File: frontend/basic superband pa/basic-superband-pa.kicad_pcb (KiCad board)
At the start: 2 copper layers, 64.4 x 78.6 mm, 69 parts, among them CN1 EDGE, CN2 BREAKOUT, K1 D3002, K2 D3002, P1 BNC, P2 CONN_02X01, P3 CONN_01X02, Q1 NPN, Q2 PNP, Q3 RD16HHF1, Q4 NPN, T1 TRANSFO, T2 8:1, T3 4:1, T4 OUT_TRANSF, U1 LP2951-50D

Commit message: Upload latest pcb changes
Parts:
- removed CN2: BREAKOUT, Pin_Headers:Pin_Header_Straight_1x12
- removed MH (x4): VAL**, HERMESLITE:MH
- removed MountingHole_2-7mm: VAL**, Mounting_Holes:MountingHole_2-7mm
- removed P3: CONN_01X02, Pin_Headers:Pin_Header_Straight_1x02
- removed Q4: NPN, Transistors_SMD:sot23
- removed R9: 4.99k, HERMESLITE:R_0805
- added C25: 0.01uF, HERMESLITE:C_0805, B.Cu at (151.2, 73.2)
- added C26: 0.01uF, HERMESLITE:C_0805, B.Cu at (158.2, 84.4)
- added C27: 0.01uF, HERMESLITE:C_0805, B.Cu at (154.4, 72.2)
- added C28: 0.01uF, HERMESLITE:C_0805, F.Cu at (183.2, 54.8)
- added C29: 0.1uF, HERMESLITE:C_0805, B.Cu at (174.6, 68.3)
- added MountingHole_3-5mm: VAL**, Mounting_Holes:MountingHole_3-5mm, F.Cu at (189.8, 90.6)
- added MountingHole_3-5mm: VAL**, Mounting_Holes:MountingHole_3-5mm, F.Cu at (139.0, 90.6)
- added MountingHole_3-5mm: VAL**, Mounting_Holes:MountingHole_3-5mm, F.Cu at (189.6, 39.6)
- added MountingHole_3-5mm: VAL**, Mounting_Holes:MountingHole_3-5mm, F.Cu at (139.0, 39.4)
- added MountingHole_6mm: VAL**, Mounting_Holes:MountingHole_6mm, F.Cu at (154.4, 50.4)
- C1, C15, C16, C2, Q1, R1, R2, R5, R7: moved to B.Cu
- C12: moved to F.Cu
- L10: footprint Choke_Axial_ThroughHole:Choke_Horizontal_RM10mm -> Choke_Toroid_ThroughHole:Choke_Toroid_horizontal_Diameter3-5mm_Amidon-T12
- moved L5 38.7 mm to (184.0, 87.0), turned to 180 degrees
- moved L2 38.2 mm to (143.6, 73.4), turned to 270 degrees
- moved L10 34.5 mm to (186.6, 44.8)
- moved L3 32.1 mm to (142.2, 86.6)
- moved C7 31.9 mm to (146.6, 91.0)
- moved C6 31.5 mm to (142.8, 85.8)
- moved L6 30.6 mm to (190.4, 85.2), turned to 90 degrees
- moved L4 29.2 mm to (156.2, 87.0), turned to 180 degrees
- moved C8 28.7 mm to (182.2, 74.6)
- moved L7 27.4 mm to (170.0, 87.0), turned to 180 degrees
- moved C13 24.3 mm to (140.0, 61.8), turned to 90 degrees
- moved C5 24.2 mm to (146.8, 84.6)
- moved C4 23.8 mm to (151.4, 83.6), turned to 180 degrees
- moved C2 17.8 mm to (136.8, 73.6), turned to 270 degrees
- moved L1 17.5 mm to (158.6, 86.6), turned to 90 degrees
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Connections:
- CN1 pad A16: Net-(CN1-PadA15) -> Net-(CN1-PadA16)
- CN1 pad A18: Net-(CN1-PadA17) -> Net-(CN1-PadA18)
- K2 pad 7: Net-(C24-Pad2) -> Net-(C29-Pad1)
- R8 pad 2: Net-(Q4-Pad3) -> PTT#
- U1 pad 3: Net-(Q4-Pad3) -> PTT#
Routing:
- net PTT#: track 36.9 -> 88.3 mm, vias 1 -> 7
- net Net-(K1-Pad7): track 46.6 -> 14.6 mm, vias 1 -> 0
- net Net-(CN1-PadA17): track 30.6 -> 0.00 mm
- net Net-(CN1-PadA15): track 30.4 -> 0.00 mm
- net Net-(CN1-PadB14): track 23.9 -> 0.00 mm, vias 1 -> 0
- net Net-(CN1-PadB18): track 21.2 -> 0.00 mm
- net Net-(CN1-PadB13): track 20.8 -> 0.00 mm, vias 1 -> 0
- net Net-(CN1-PadB17): track 20.7 -> 0.00 mm
- net Net-(CN1-PadB16): track 19.9 -> 0.00 mm
- net Net-(CN1-PadB15): track 19.3 -> 0.00 mm
- net Net-(C19-Pad2): track 41.4 -> 23.1 mm
- net GPIO0: track 44.1 -> 26.0 mm, vias 2 -> 0
- net Net-(Q4-Pad3): track 17.5 -> 0.00 mm
- net Net-(CN1-PadB3): track 12.4 -> 29.4 mm
- net Net-(K1-Pad8): track 31.9 -> 15.9 mm
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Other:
- board size 64.4 x 78.6 mm -> 64.5 x 60 mm

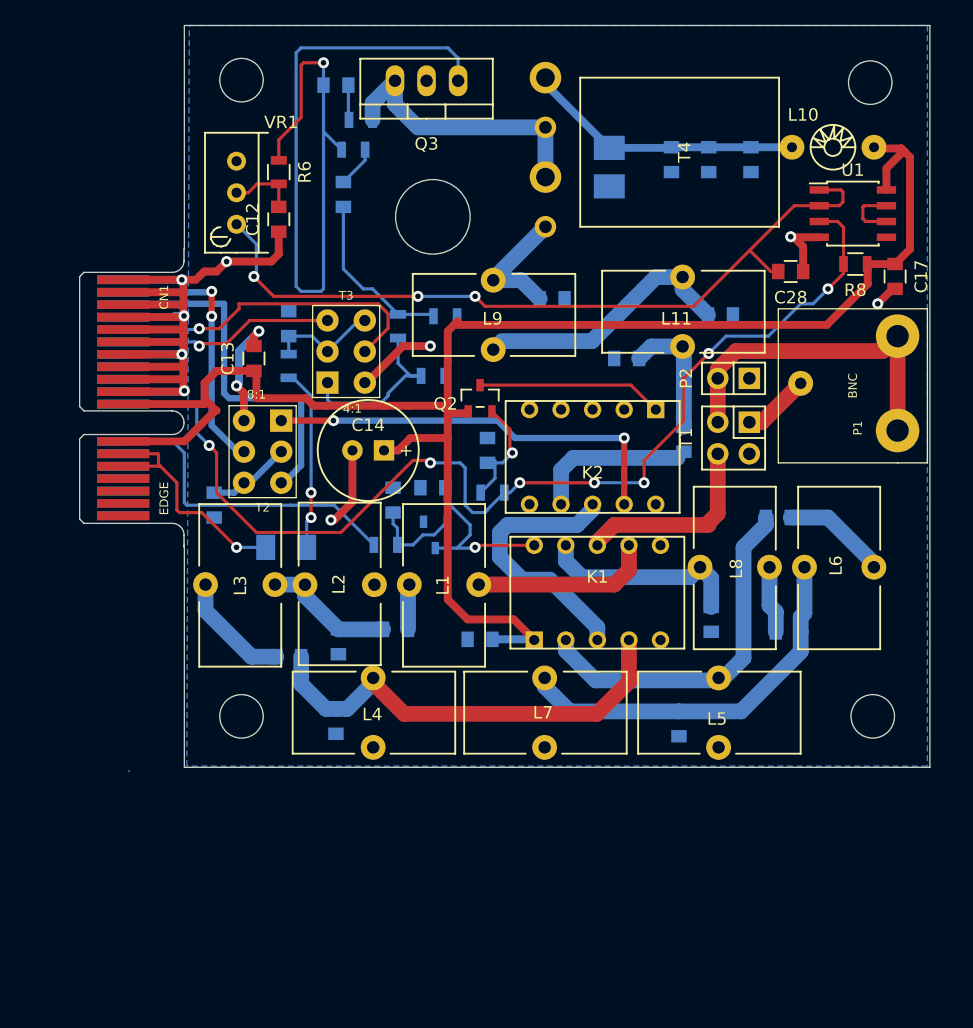
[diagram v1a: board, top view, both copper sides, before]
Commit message: Correct compnent naming and fix relay error
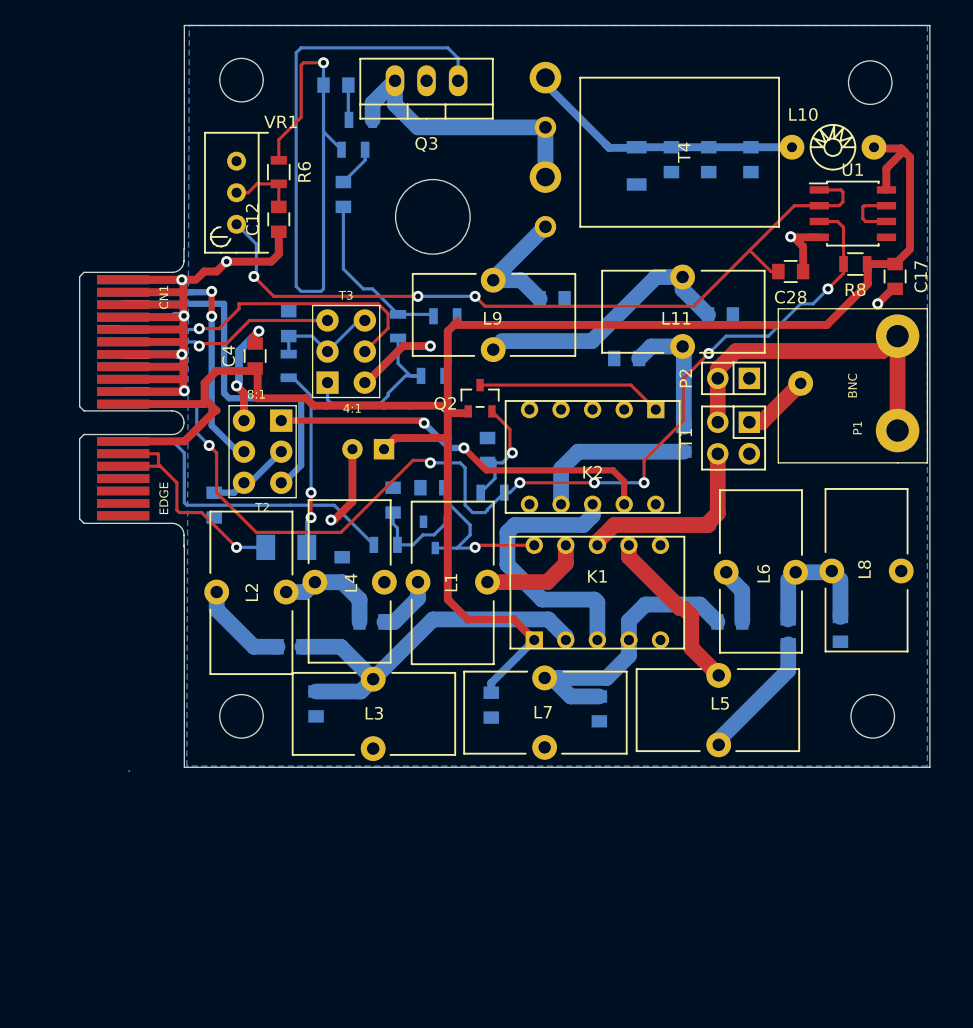
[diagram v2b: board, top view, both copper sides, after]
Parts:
- C13: value 0.1uF -> C; moved to B.Cu
- C14: value 47uF 16V -> C; footprint Discret:C1V8 -> HERMESLITE:C_0805; moved to B.Cu
- C22: footprint Capacitors_Tantalum_SMD:TantalC_SizeB_EIA-3528_Reflow -> Capacitors_SMD:C_1206
- C4: value C -> 0.1uF; moved to F.Cu
- C7: value C -> 47uF 16V; footprint HERMESLITE:C_0805 -> Discret:C1V8
- moved C13 52.0 mm to (187.2, 83.6), turned to 270 degrees
- moved C8 35.4 mm to (147.1, 78.8), turned to 90 degrees
- moved C9 29.2 mm to (145.0, 89.6)
- moved C14 27.9 mm to (167.8, 90.0), turned to 270 degrees
- moved C4 24.7 mm to (140.1, 61.6), turned to 90 degrees
- moved C7 22.1 mm to (149.2, 69.1), turned to 180 degrees
- moved L6 18.2 mm to (177.5, 72.4), turned to 270 degrees
- moved L4 18.2 mm to (144.4, 73.2), turned to 270 degrees
- moved L5 14.7 mm to (170.8, 93.4), turned to 0 degrees
- moved L3 14.0 mm to (156.2, 87.1), turned to 180 degrees
- moved L2 13.8 mm to (143.1, 87.2), turned to 90 degrees
- moved L8 13.5 mm to (186.0, 72.3), turned to 270 degrees
- moved C26 5.38 mm to (159.1, 89.7), turned to 90 degrees
- moved C5 3.14 mm to (149.5, 83.0), turned to 180 degrees
- moved C22 2.20 mm to (170.8, 46.3)
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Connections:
- C11 pad 2: GND -> Net-(C11-Pad2)
- C13 pad 1: Net-(C13-Pad1) -> Net-(C10-Pad1)
- C14 pad 1: Net-(C13-Pad1) -> Net-(C11-Pad1)
- C17 pad 1: Net-(C13-Pad1) -> Net-(C17-Pad1)
- C26 pad 2: Net-(C13-Pad1) -> Net-(C17-Pad1)
- C4 pad 1: Net-(C4-Pad1) -> Net-(C17-Pad1)
- C4 pad 2: Net-(C4-Pad2) -> GND
- C5 pad 1: Net-(C4-Pad2) -> Net-(C5-Pad1)
- C5 pad 2: GND -> Net-(C5-Pad2)
- C7 pad 1: Net-(C6-Pad2) -> Net-(C17-Pad1)
- C8 pad 1: Net-(C8-Pad1) -> Net-(C5-Pad2)
- C8 pad 2: Net-(C8-Pad2) -> GND
- C9 pad 1: Net-(C10-Pad1) -> Net-(C6-Pad2)
- CN1 pad A11: Net-(C13-Pad1) -> Net-(C17-Pad1)
- CN1 pad A12: Net-(C13-Pad1) -> Net-(C17-Pad1)
- K1 pad 1: Net-(C13-Pad1) -> Net-(C17-Pad1)
- K1 pad 2: Net-(C8-Pad1) -> Net-(C6-Pad2)
- K1 pad 4: Net-(C6-Pad2) -> Net-(C11-Pad1)
- K1 pad 9: Net-(C11-Pad1) -> Net-(K1-Pad9)
- L1 pad 1: Net-(K1-Pad7) -> Net-(K1-Pad9)
- L1 pad 2: Net-(C4-Pad1) -> Net-(C5-Pad1)
- L10 pad 1: Net-(C13-Pad1) -> Net-(C17-Pad1)
- L2 pad 1: Net-(C4-Pad2) -> Net-(C5-Pad2)
- L2 pad 2: GND -> Net-(C6-Pad1)
- L3 pad 1: Net-(C4-Pad2) -> Net-(C6-Pad2)
- L3 pad 2: Net-(C6-Pad1) -> GND
- L4 pad 1: Net-(C6-Pad2) -> Net-(C5-Pad2)
- L5 pad 1: Net-(C8-Pad1) -> Net-(C10-Pad2)
- L5 pad 2: GND -> Net-(K1-Pad7)
- L6 pad 1: Net-(C8-Pad2) -> Net-(C11-Pad2)
- L7 pad 1: Net-(C10-Pad1) -> Net-(C11-Pad1)
- L8 pad 1: Net-(C10-Pad2) -> Net-(C10-Pad1)
- L8 pad 2: Net-(C11-Pad1) -> GND
- Q2 pad 1: Net-(C13-Pad1) -> Net-(C17-Pad1)
- R8 pad 1: Net-(C13-Pad1) -> Net-(C17-Pad1)
- U1 pad 8: Net-(C13-Pad1) -> Net-(C17-Pad1)
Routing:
- net Net-(C17-Pad1): track 0.00 -> 139.9 mm
- net Net-(C13-Pad1): track 137.1 -> 0.00 mm
- net Net-(C8-Pad1): track 28.9 -> 0.00 mm
- net Net-(C10-Pad1): track 31.0 -> 11.0 mm
- net Net-(C4-Pad2): track 10.7 -> 0.00 mm
- net Net-(C5-Pad2): track 0.00 -> 8.91 mm
- net Net-(K1-Pad9): track 0.00 -> 8.66 mm
- net Net-(C8-Pad2): track 8.53 -> 0.00 mm
- net Net-(C11-Pad1): track 16.5 -> 23.6 mm
- net Net-(C6-Pad2): track 35.7 -> 30.1 mm
- net Net-(C10-Pad2): track 5.41 -> 10.4 mm
- net Net-(C5-Pad1): track 0.00 -> 4.79 mm
- net Net-(C11-Pad2): track 0.00 -> 4.53 mm
- net Net-(C4-Pad1): track 3.65 -> 0.00 mm
- net Net-(K2-Pad9): track 33.5 -> 31.5 mm
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
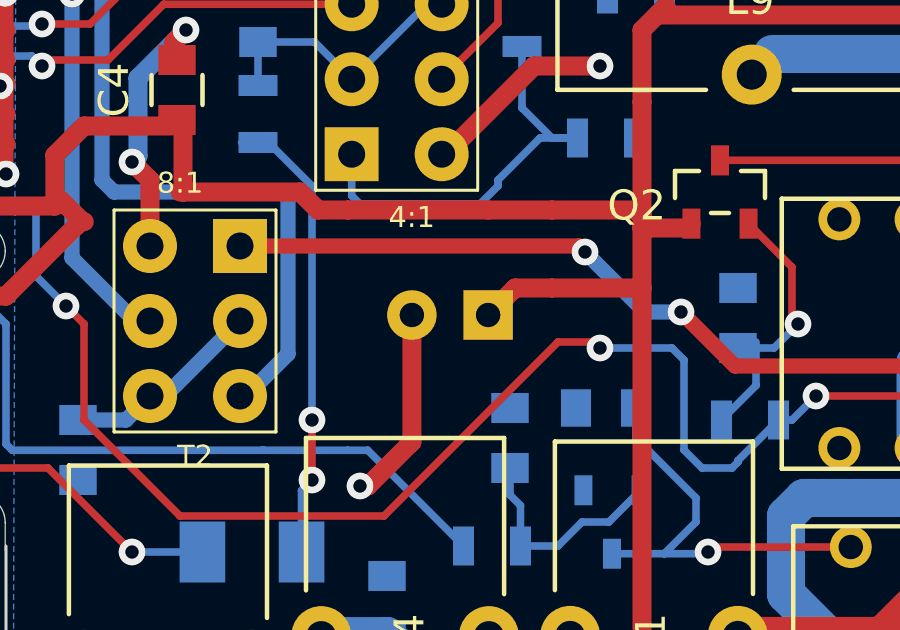
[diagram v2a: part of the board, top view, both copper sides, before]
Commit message: Minor silkscreen bug
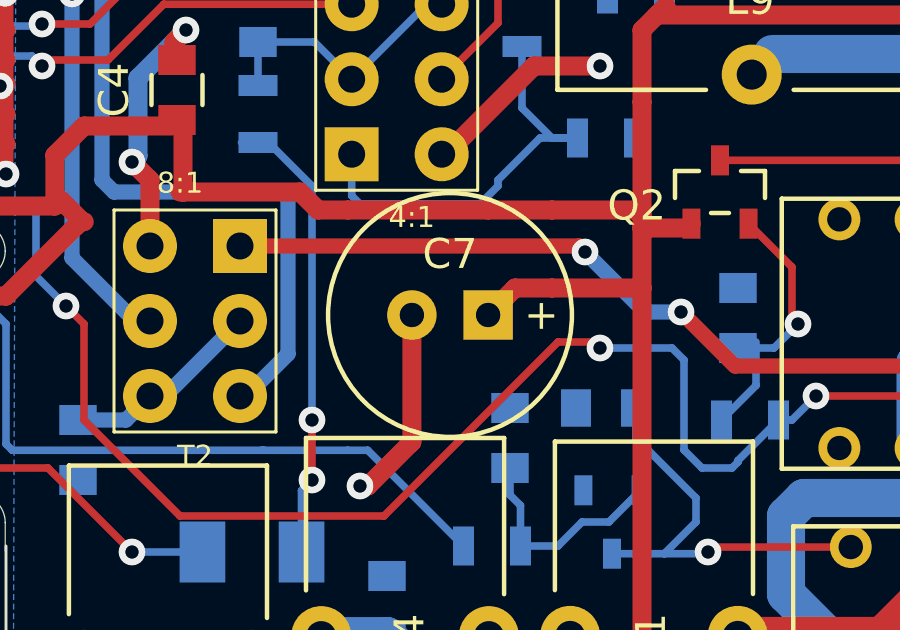
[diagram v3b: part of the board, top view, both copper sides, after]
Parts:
- C7: moved to F.Cu
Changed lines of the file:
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@@
     (links 138)
     (no_connects 0)
-    (area 129.98958 34.949999 194.450001 95.056161)
+    (area 125.47056 33.72012 198.438524 96.969)
     (thickness 1.6)
     (drawings 6)
@@
     )
   )
-  (module Discret:C1V8 (layer B.Cu)
+  (module Discret:C1V8 (layer F.Cu)
     (at 149.2 69.1 180)
-    (fp_text reference C7 (at 0 -2.032 180) (layer B.SilkS)
-      (effects (font (size 1 1) (thickness 0.15)) (justify mirror))
-    )
-    (fp_text value "47uF 16V" (at 0 1.77546 270) (layer B.SilkS)
-      (effects (font (size 1 1) (thickness 0.15)) (justify mirror))
-    )
-    (fp_text user + (at -3.04546 0 180) (layer B.SilkS)
-      (effects (font (size 1 1) (thickness 0.15)) (justify mirror))
-    )
-    (fp_circle (center 0 0) (end 4.064 0) (layer B.SilkS) (width 0.15))
-    (pad 1 thru_hole rect (at -1.27 0 180) (size 1.651 1.651) (drill 0.8128) (layers *.Cu *.Mask B.SilkS)
+    (fp_text reference C7 (at 0 2.032 180) (layer F.SilkS)
+      (effects (font (size 1 1) (thickness 0.15)))
+    )
+    (fp_text value "47uF 16V" (at 0 -1.77546 450) (layer F.SilkS) hide
+      (effects (font (size 1 1) (thickness 0.15)))
+    )
+    (fp_text user + (at -3.04546 0 180) (layer F.SilkS)
+      (effects (font (size 1 1) (thickness 0.15)))
+    )
+    (fp_circle (center 0 0) (end 4.064 0) (layer F.SilkS) (width 0.15))
+    (pad 1 thru_hole rect (at -1.27 0 180) (size 1.651 1.651) (drill 0.8128) (layers *.Cu *.Mask F.SilkS)
       (net 57 "Net-(C17-Pad1)"))
-    (pad 2 thru_hole circle (at 1.27 0 180) (size 1.651 1.651) (drill 0.8128) (layers *.Cu *.Mask B.SilkS)
+    (pad 2 thru_hole circle (at 1.27 0 180) (size 1.651 1.651) (drill 0.8128) (layers *.Cu *.Mask F.SilkS)
       (net 2 GND))
     (model Discret/C1V8.wrl
@@
     (tags "capacitor 1206")
     (attr smd)
-    (fp_text reference C22 (at 0 2.3 270) (layer B.SilkS)
-      (effects (font (size 1 1) (thickness 0.15)) (justify mirror))
-    )
-    (fp_text value "10uF 16V" (at 0 -2.3 270) (layer B.SilkS)
-      (effects (font (size 1 1) (thickness 0.15)) (justify mirror))
-    )
+    (fp_text reference C22 (at 4 -0.1 270) (layer B.SilkS)
+      (effects (font (size 1 1) (thickness 0.15)) (justify mirror))
+    )
+    (fp_text value "10uF 16V" (at 0 -2.3 270) (layer B.SilkS) hide
+      (effects (font (size 1 1) (thickness 0.15)) (justify mirror))
+    )

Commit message: Final PCB, hopefully
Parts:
- added G***: OSHW-logo_copper-front_3mm, OSHW:OSHW-logo_copper-front_3mm, F.Cu at (184.1, 39.5)
- moved R12 7.56 mm to (158.5, 65.3)
- moved L9 6.21 mm to (160.6, 51.7), turned to 270 degrees
- moved R11 5.40 mm to (151.4, 64.6)
- moved C18 5.00 mm to (164.2, 62.0)
- moved MountingHole_6mm 4.41 mm to (154.7, 54.8)
- moved R10 2.01 mm to (154.2, 65.2)
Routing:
- net Net-(C15-Pad2): track 13.8 -> 24.3 mm
- net Net-(C23-Pad2): track 21.6 -> 13.0 mm
- net GND: track 119.9 -> 127.4 mm, vias 11 -> 12
- net Net-(R10-Pad2): track 14.7 -> 9.88 mm
- net Net-(C28-Pad2): track 62.6 -> 65.4 mm, vias 3 -> 1
- net Net-(C18-Pad2): track 10.4 -> 12.6 mm
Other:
- net class Microstrip: trace_width 3.81 -> 0.381
- board text added: "Hermes Lite Superband PA 1.0 © 2015 AC9HY"

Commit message: More pcb changes
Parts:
- C15, C16, R5, R7: moved to F.Cu
- moved R7 7.56 mm to (155.5, 45.7)
- moved C16 6.59 mm to (151.0, 44.7)
- moved C8 4.39 mm to (146.2, 83.1), turned to 270 degrees
- moved C6 2.69 mm to (141.0, 86.9)
- moved FB1 1.40 mm to (142.6, 75.6)
- moved C15 0.94 mm to (147.7, 49.4)
- moved MountingHole_6mm 0.81 mm to (153.9, 54.7)
- moved R5 0.76 mm to (147.7, 45.7), turned to 270 degrees
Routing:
- net GND: track 127.4 -> 107.7 mm, vias 12 -> 9
- net Net-(C15-Pad2): track 24.3 -> 35.5 mm, vias 0 -> 1
- net Net-(C28-Pad2): track 65.4 -> 61.0 mm
- net Net-(C17-Pad1): track 139.9 -> 136.7 mm
- net Net-(C5-Pad2): track 8.91 -> 11.7 mm
- net Net-(C16-Pad2): track 67.9 -> 70.2 mm, vias 1 -> 2
- net Net-(C15-Pad1): track 3.37 -> 1.75 mm
- net Net-(K1-Pad3): track 22.9 -> 21.3 mm
- net GPIO0: track 26.0 -> 24.7 mm, vias 0 -> 2
- net Net-(C6-Pad2): track 30.1 -> 31.3 mm
- net Net-(FB1-Pad2): track 15.3 -> 14.2 mm, vias 2 -> 0
- net Net-(Q3-Pad3): track 22.7 -> 21.7 mm
- net PTT#: track 88.3 -> 89.3 mm, vias 7 -> 8

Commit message: Few more pcb changes
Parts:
- added JP1: JUMPER4, HERMESLITE:JUMPER4, F.Cu at (156.2, 90.4)
- added R13: 4.99k, HERMESLITE:R_0805, B.Cu at (162.4, 89.0)
- moved C26 7.56 mm to (156.5, 82.6), turned to 0 degrees
- moved L7 4.01 mm to (174.0, 86.7)
- moved C14 3.91 mm to (171.7, 89.7)
- moved L5 3.20 mm to (174.0, 93.3)
- moved C6 2.81 mm to (140.8, 84.1)
- moved L3 1.58 mm to (154.7, 86.6)
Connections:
- R1 pad 2: GPIO0 -> Net-(JP1-Pad2)
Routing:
- net Net-(JP1-Pad2): track 0.00 -> 23.6 mm, vias 0 -> 1
- net GPIO0: track 24.7 -> 45.7 mm, vias 2 -> 3
- net Net-(C17-Pad1): track 136.7 -> 141.8 mm
- net Net-(C11-Pad1): track 23.6 -> 19.4 mm
- net Net-(K1-Pad7): track 13.6 -> 16.9 mm
- net Net-(JP1-Pad3): track 0.00 -> 3.18 mm
- net Net-(C6-Pad1): track 7.54 -> 4.66 mm
- net Net-(C6-Pad2): track 31.3 -> 29.5 mm
- net Net-(C10-Pad2): track 10.4 -> 8.98 mm
